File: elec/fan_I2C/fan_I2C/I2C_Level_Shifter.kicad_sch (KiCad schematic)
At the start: 21 parts, among them J201 0.100_2Pin, J202 S04B-XASK-1(LF)(SN), Q201 BSS138, Q202 BSS138

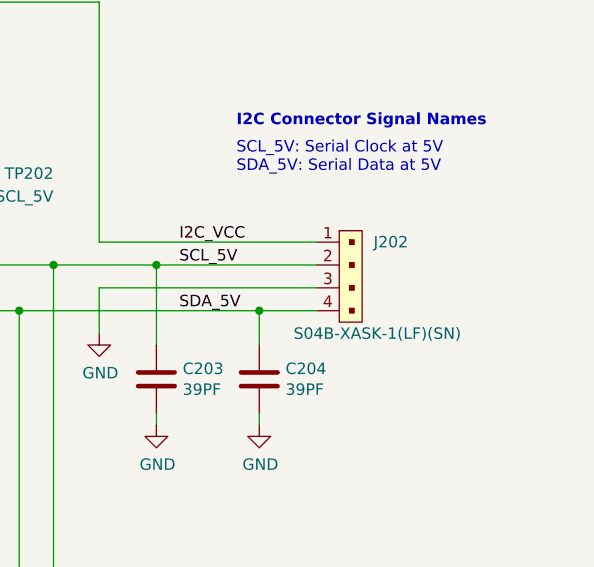
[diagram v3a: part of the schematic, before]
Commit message: Add connect Due 3V3, 5V and gnd.
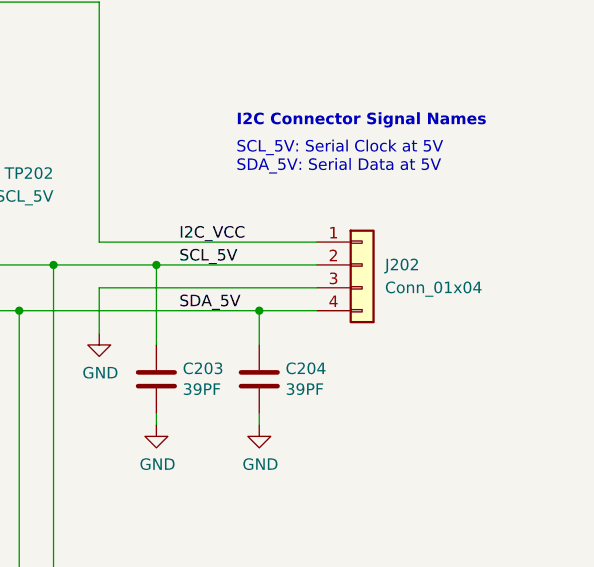
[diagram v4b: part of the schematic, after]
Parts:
- removed J202: S04B-XASK-1(LF)(SN), PubInv_PCB:S04B-XASK-1(LF)(SN), symbol GPAD_SCH_LIB:S04B-XASK-1(LF)(SN)
- added J202: Conn_01x04, Connector_PinHeader_2.54mm:PinHeader_1x04_P2.54mm_Vertical, symbol Connector_Generic:Conn_01x04
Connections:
- net GND: now also J202.3 (Pin_3)
- net I2C_VCC: now also J202.1 (Pin_1)
- net SCL_5V: now also J202.2 (Pin_2)
- net SDA_5V: now also J202.4 (Pin_4)
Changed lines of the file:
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@@
     (pin "3")
-  )
-  (symbol (lib_id "GPAD_SCH_LIB:S04B-XASK-1(LF)(SN)") (at 243.84 83.82 90) (mirror x) (unit 1)
-    (in_bom yes) (on_board yes)
-    (property "Reference" "J202" (id 0) (at 247.65 83.82 90)
-      (effects (font (size 1.27 1.27)) (justify right))
-    )
-    (property "Value" "S04B-XASK-1(LF)(SN)" (id 1) (at 238.76 93.98 90)
-      (effects (font (size 1.27 1.27)) (justify right))
-    )
-    (property "Footprint" "PubInv_PCB:S04B-XASK-1(LF)(SN)" (id 2) (at 238.76 88.9 0)
-      (effects (font (size 1.524 1.524)) (justify left) hide)
-    )
-    (property "Datasheet" "https://www.jst-mfg.com/product/pdf/eng/eXA1.pdf" (id 3) (at 236.22 88.9 0)
-      (effects (font (size 1.524 1.524)) (justify left) hide)
-    )
-    (property "Digi-Key_PN" "455-4090-ND" (id 4) (at 233.68 88.9 0)
-      (effects (font (size 1.524 1.524)) (justify left) hide)
-    )
-    (property "MPN" "S04B-XASK-1(LF)(SN)" (id 5) (at 231.14 88.9 0)
-      (effects (font (size 1.524 1.524)) (justify left) hide)
-    )
-    (property "Category" "Connectors, Interconnects" (id 6) (at 228.6 88.9 0)
-      (effects (font (size 1.524 1.524)) (justify left) hide)
-    )
-    (property "Family" "Rectangular Connectors - Headers, Male Pins, Side Entery" (id 7) (at 226.06 88.9 0)
-      (effects (font (size 1.524 1.524)) (justify left) hide)
-    )
-    (property "Description" "CONN HEADER R/A 4POS 2.5MM" (id 8) (at 218.44 88.9 0)
-      (effects (font (size 1.524 1.524)) (justify left) hide)
-    )
-    (property "Manufacturer" "JST Sales America" (id 9) (at 215.9 88.9 0)
-      (effects (font (size 1.524 1.524)) (justify left) hide)
-    )
-    (property "Status" "Active" (id 10) (at 213.36 88.9 0)
-      (effects (font (size 1.524 1.524)) (justify left) hide)
-    )
-    (property "Distributor 1" "JLCPCB" (id 11) (at 243.84 83.82 0)
-      (effects (font (size 1.27 1.27)) hide)
-    )
-    (property "Distributor 1 PN" "C265097" (id 12) (at 243.84 83.82 0)
-      (effects (font (size 1.27 1.27)) hide)
-    )
-    (property "Distributor 2" "DigiKey  " (id 13) (at 243.84 83.82 0)
-      (effects (font (size 1.27 1.27)) hide)
-    )
-    (property "Distributor 2 PN" "455-4090-ND" (id 14) (at 247.0912 89.8144 90)
-      (effects (font (size 1.27 1.27)) (justify right) hide)
-    )
-    (property "AssemblyType" "HAND" (id 16) (at 243.84 83.82 0)
-      (effects (font (size 1.27 1.27)) hide)
-    )
-    (property "Cost" "0.1517" (id 17) (at 243.84 83.82 0)
-      (effects (font (size 1.27 1.27)) hide)
-    )
-    (property "LongLead" "YES" (id 18) (at 243.84 83.82 0)
-      (effects (font (size 1.27 1.27)) hide)
-    )
-    (pin "1")
-    (pin "2")
-    (pin "3")
-    (pin "4")
   )
   (symbol (lib_id "Device:R") (at 212.09 33.02 90) (unit 1)
@@
     (pin "2")
   )
+  (symbol (lib_id "Connector_Generic:Conn_01x04") (at 246.38 86.36 0) (unit 1)
+    (in_bom yes) (on_board yes) (fields_autoplaced)
+    (property "Reference" "J202" (id 0) (at 248.92 86.3599 0)
+      (effects (font (size 1.27 1.27)) (justify left))
+    )
+    (property "Value" "Conn_01x04" (id 1) (at 248.92 88.8999 0)
+      (effects (font (size 1.27 1.27)) (justify left))
+    )
+    (property "Footprint" "Connector_PinHeader_2.54mm:PinHeader_1x04_P2.54mm_Vertical" (id 2) (at 246.38 86.36 0)
+      (effects (font (size 1.27 1.27)) hide)
+    )
+    (property "Datasheet" "~" (id 3) (at 246.38 86.36 0)
+      (effects (font (size 1.27 1.27)) hide)
+    )
+    (pin "1")
+    (pin "2")
+    (pin "3")
+    (pin "4")
+  )
   (symbol (lib_id "Device:R") (at 212.09 25.4 90) (unit 1)
